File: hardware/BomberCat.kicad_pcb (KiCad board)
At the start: 2 copper layers, 65 x 84.7 mm, 111 parts, among them J1 Battery, J3 MAGSPOOF, J4 MAGSPOOF, P1 USB_C_Plug_USB2.0, Q1 DMG3415U-7, SW1 RESET, SW2 GPIO, SW3 ON, SW4 SOURCE MAG, U1 PN7150B0HN_C11002E-PN7150B0HN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

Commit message: fix(hw):update labels
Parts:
- removed kibuzzard-62EEB073: G***, kibuzzard-62EEB073
- removed kibuzzard-64382690: G***, kibuzzard-64382690
- added kibuzzard-67FEA661: G***, kibuzzard-67FEA661, B.Cu at (108.3, 145.5)
- added kibuzzard-67FEA7C0: G***, kibuzzard-67FEA7C0, B.Cu at (147.3, 150.3)

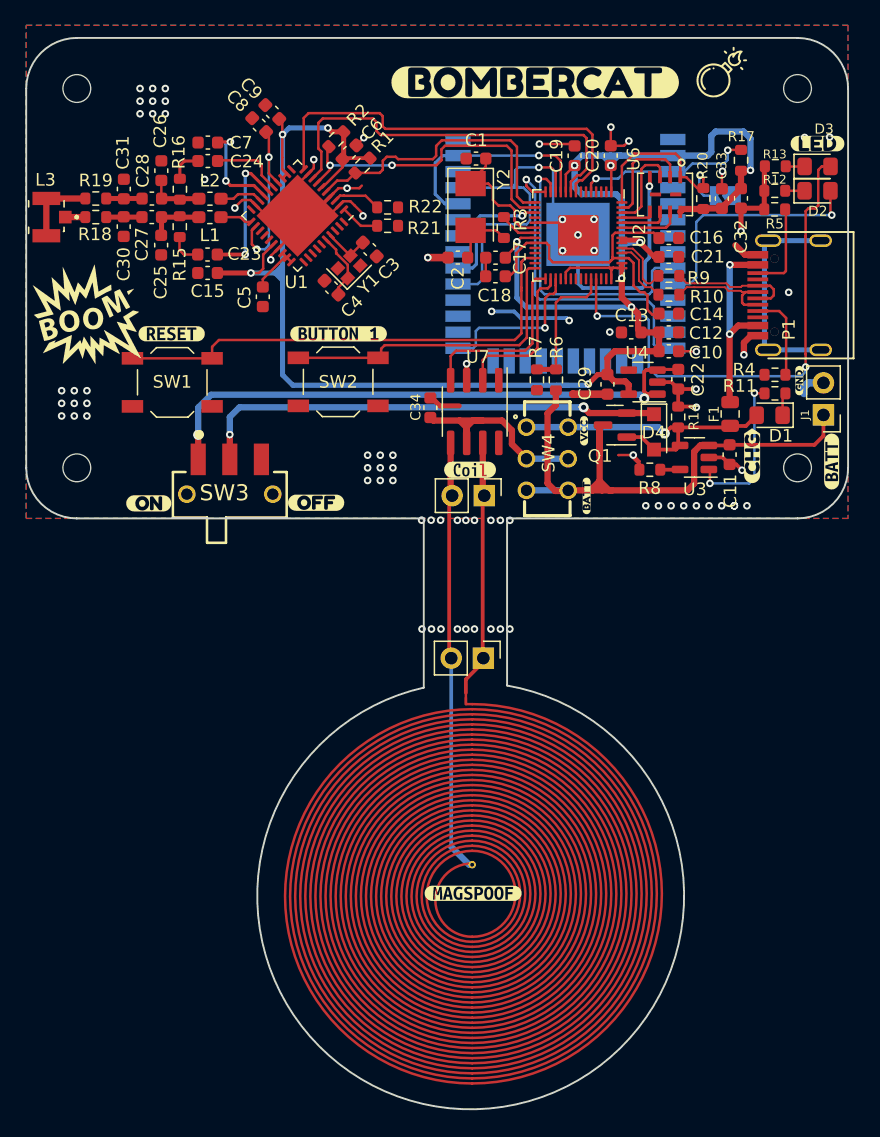
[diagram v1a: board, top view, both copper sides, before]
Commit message: feat(hw): update tracks, remove switch position change and resize coil arm,
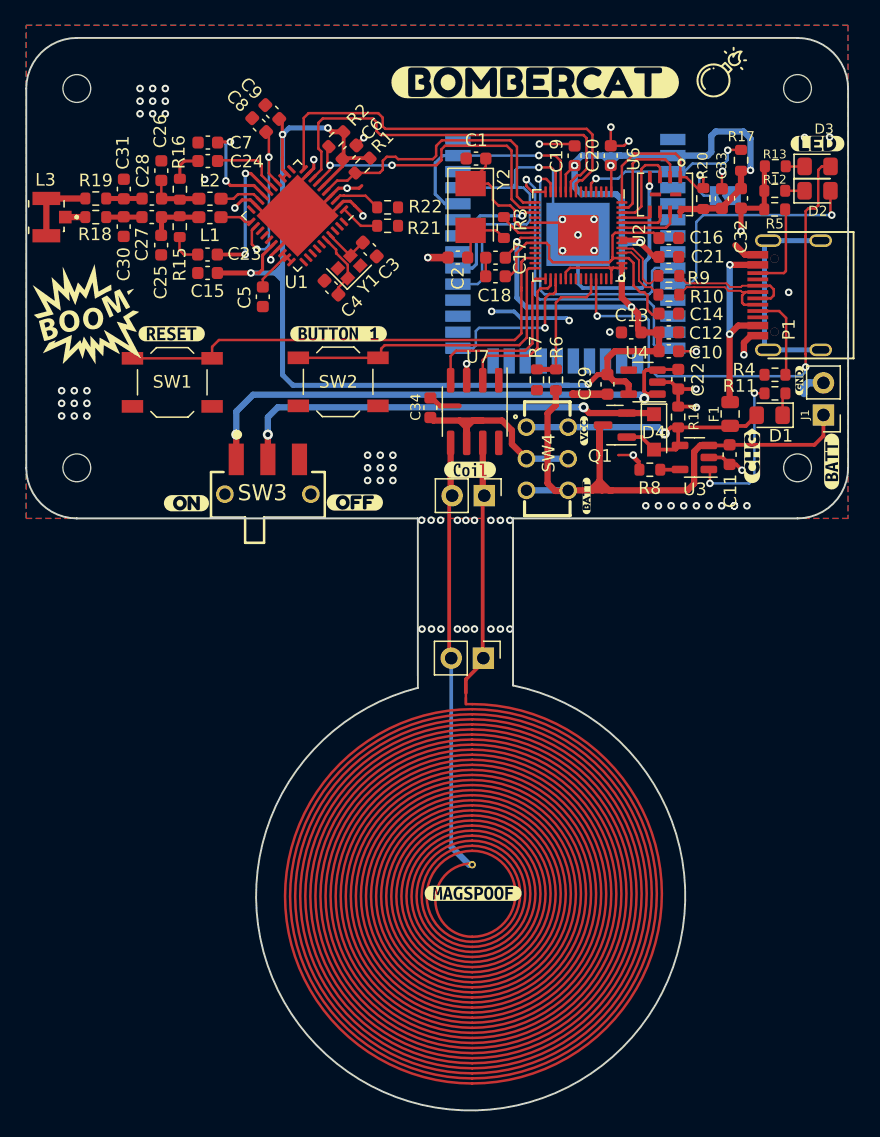
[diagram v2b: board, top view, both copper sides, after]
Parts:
- moved kibuzzard-67F6E601 3.06 mm to (118.0, 172.7)
- moved SW3 3.01 mm to (111.1, 170.3)
- moved kibuzzard-67F6E5D9 2.98 mm to (104.7, 172.8)
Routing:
- net Net-(SW3-A): track 46.6 -> 43.4 mm
- net Net-(D4-K): track 37.4 -> 34.5 mm
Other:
- board size 65 x 84.7 mm -> 65 x 84.8 mm

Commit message: fix(hw): update tracks width
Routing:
- net GND: track 124.8 -> 122.5 mm
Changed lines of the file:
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@@
 				(font
 					(size 0.001 0.001)
+					(thickness 0.15)
 				)
 				(justify mirror)
@@
 				(font
 					(size 0.001 0.001)
+					(thickness 0.15)
 				)
 				(justify mirror)
@@
 				(font
 					(size 0.001 0.001)
+					(thickness 0.15)
 				)
 				(justify mirror)
@@
 				(font
 					(size 0.001 0.001)
+					(thickness 0.15)
 				)
 				(justify mirror)
@@
 	)
 	(segment
+		(start 140.494216 169.474216)
+		(end 140.01 168.99)
+		(width 0.2)
+		(layer "F.Cu")
+		(net 2)
+	)
+	(segment
 		(start 126.835 161.775)
 		(end 126.83 161.77)
@@
 	)
 	(segment
-		(start 140.494216 170.149118)
-		(end 140.494216 169.474216)
-		(width 0.2)
-		(layer "F.Cu")
-		(net 2)
-	)
-	(segment
 		(start 123.761618 153.371618)
 		(end 123.76 153.37)
@@
 	)
 	(segment
-		(start 138.854216 168.989118)
-		(end 138.849216 168.994118)
-		(width 0.2)
-		(layer "F.Cu")
-		(net 2)
-	)
-	(segment
 		(start 109.735126 148.81)
 		(end 109.09 148.81)
@@
 	)
 	(segment
+		(start 140.494216 170.149118)
+		(end 140.494216 169.474216)
+		(width 0.2)
+		(layer "F.Cu")
+		(net 2)
+	)
+	(segment
 		(start 125.361716 153.371618)
 		(end 123.761618 153.371618)
@@
 	)
 	(segment
-		(start 140.494216 169.474216)
-		(end 140.01 168.99)
-		(width 0.2)
-		(layer "F.Cu")
-		(net 2)
-	)
-	(segment
-		(start 139.749216 168.989118)
-		(end 138.854216 168.989118)
-		(width 0.2)
-		(layer "F.Cu")
-		(net 2)
-	)
-	(segment
 		(start 141.919216 163.219118)
 		(end 143.019216 163.219118)
@@
 	)
 	(segment
-		(start 140.494216 170.149118)
-		(end 140.494216 169.734118)
-		(width 0.2)
-		(layer "F.Cu")
-		(net 2)
-	)
-	(segment
 		(start 124.714 165.1)
 		(end 126.238 165.1)
@@
 	)
 	(segment
-		(start 140.494216 169.734118)
-		(end 139.749216 168.989118)
-		(width 0.2)
-		(layer "F.Cu")
-		(net 2)
-	)
-	(segment
 		(start 111.913204 152.667456)
 		(end 113.46 151.12066)
@@
 		(start 155.05 167.47)
 		(end 155.05 165.82)
-		(width 0.3)
+		(width 0.5)
 		(layer "F.Cu")
 		(net 10)
@@
 		(start 145.986716 168.229118)
 		(end 147.579216 168.229118)
-		(width 0.3)
+		(width 0.5)
 		(layer "F.Cu")
 		(net 10)
@@
 		(start 147.629216 168.179118)
 		(end 154.340882 168.179118)
-		(width 0.3)
+		(width 0.5)
 		(layer "F.Cu")
 		(net 10)
@@
 		(start 154.340882 168.179118)
 		(end 155.05 167.47)
-		(width 0.3)
+		(width 0.5)
 		(layer "F.Cu")
 		(net 10)
@@
 		(start 147.579216 168.229118)
 		(end 147.629216 168.179118)
-		(width 0.3)
+		(width 0.5)
 		(layer "F.Cu")
 		(net 10)
@@
 		(start 142.975882 166.804118)
 		(end 142.5 167.28)
-		(width 0.3)
+		(width 0.5)
 		(layer "F.Cu")
 		(net 22)
@@
 		(start 143.381716 168.559118)
 		(end 143.711716 168.229118)
-		(width 0.3)
+		(width 0.5)
 		(layer "F.Cu")
 		(net 22)
@@
 		(start 141.649216 168.559118)
 		(end 143.381716 168.559118)
-		(width 0.3)
+		(width 0.5)
 		(layer "F.Cu")
 		(net 22)
@@
 		(start 143.559216 166.804118)
 		(end 142.975882 166.804118)
-		(width 0.3)
+		(width 0.5)
 		(layer "F.Cu")
 		(net 22)
@@
 		(start 139.496716 167.569118)
 		(end 140.659216 167.569118)
-		(width 0.3)
+		(width 0.5)
 		(layer "F.Cu")
 		(net 22)
@@
 		(start 148.920882 166.689118)
 		(end 149.77 165.84)
-		(width 0.3)
+		(width 0.5)
 		(layer "F.Cu")
 		(net 22)
@@
 		(start 147.514216 166.804118)
 		(end 147.629216 166.689118)
-		(width 0.3)
+		(width 0.5)
 		(layer "F.Cu")
 		(net 22)
@@
 		(start 140.659216 167.569118)
 		(end 141.649216 168.559118)
-		(width 0.3)
+		(width 0.5)
 		(layer "F.Cu")
 		(net 22)
@@
 		(start 143.559216 166.804118)
 		(end 143.559216 168.076618)
-		(width 0.3)
+		(width 0.5)
 		(layer "F.Cu")
 		(net 22)
@@
 		(start 143.559216 166.804118)
 		(end 147.514216 166.804118)
-		(width 0.3)
+		(width 0.5)
 		(layer "F.Cu")
 		(net 22)
@@
 		(start 147.629216 166.689118)
 		(end 148.920882 166.689118)
-		(width 0.3)
+		(width 0.5)
 		(layer "F.Cu")
 		(net 22)
@@
 		(start 143.559216 168.076618)
 		(end 143.711716 168.229118)
-		(width 0.3)
+		(width 0.5)
 		(layer "F.Cu")
 		(net 22)
@@
 		(start 151.82 165.84)
 		(end 151.82 164.33)
-		(width 0.2)
+		(width 0.25)
 		(layer "F.Cu")
 		(net 23)
@@
 		(start 151.82 164.33)
 		(end 152.04 164.11)
-		(width 0.2)
+		(width 0.25)
 		(layer "F.Cu")
 		(net 23)

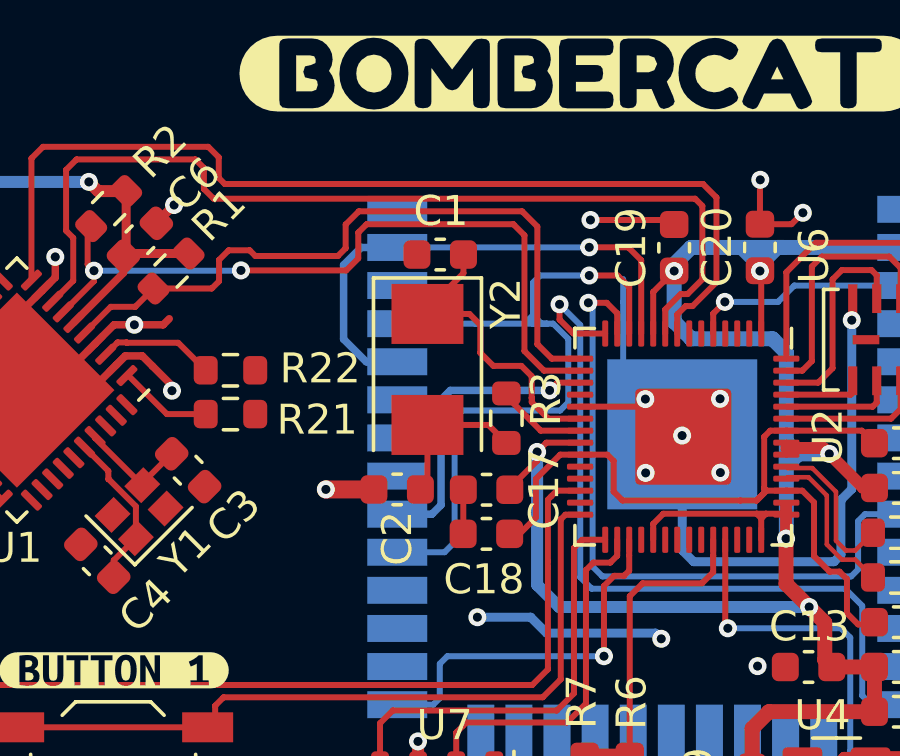
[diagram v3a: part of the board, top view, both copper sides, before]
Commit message: feat(Hw):Update_BoM
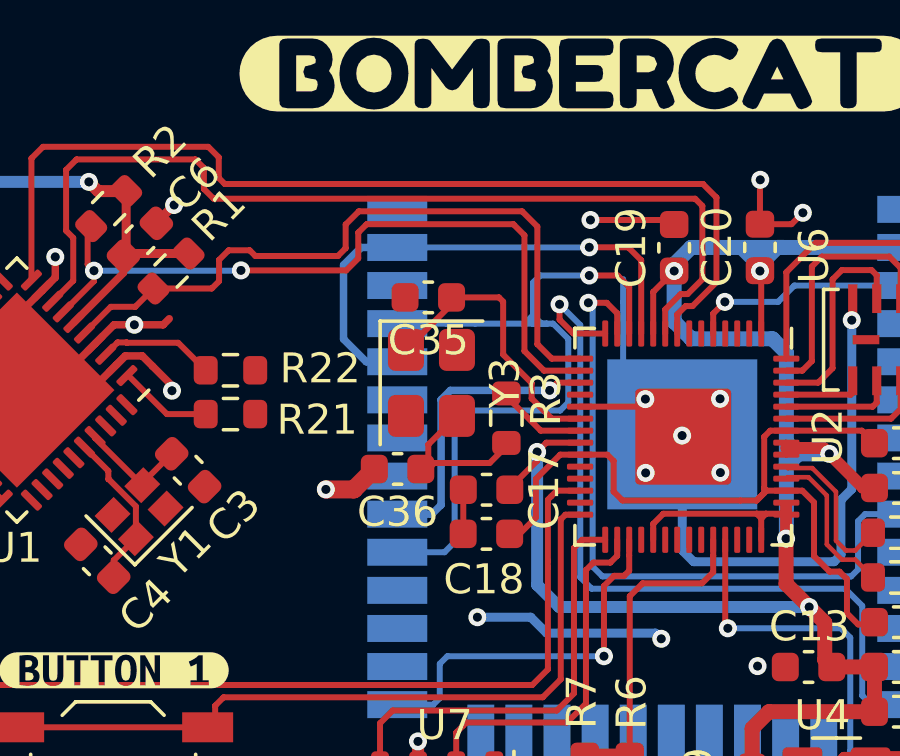
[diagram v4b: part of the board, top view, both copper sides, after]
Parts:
- removed C1, C2: 27pF, Capacitor_SMD:C_0603_1608Metric
- removed Y2: 12Mhz, Crystal:Crystal_SMD_5032-2Pin_5.0x3.2mm
- added C35: 15pF, Capacitor_SMD:C_0603_1608Metric, F.Cu at (127.2, 147.0)
- added C36: 15pF, Capacitor_SMD:C_0603_1608Metric, F.Cu at (126.2, 152.7)
- added Y3: ABM8-272-T3, Crystal:Crystal_SMD_Abracon_ABM8G-4Pin_3.2x2.5mm, F.Cu at (127.3, 149.8)
- C34: value 10uf -> 10uF
- U1: value PN7150B0HN_C11002E-PN7150B0HN_C11002E -> PN7150B0HN_C11006Y-PN7150B0HN_C11006Y

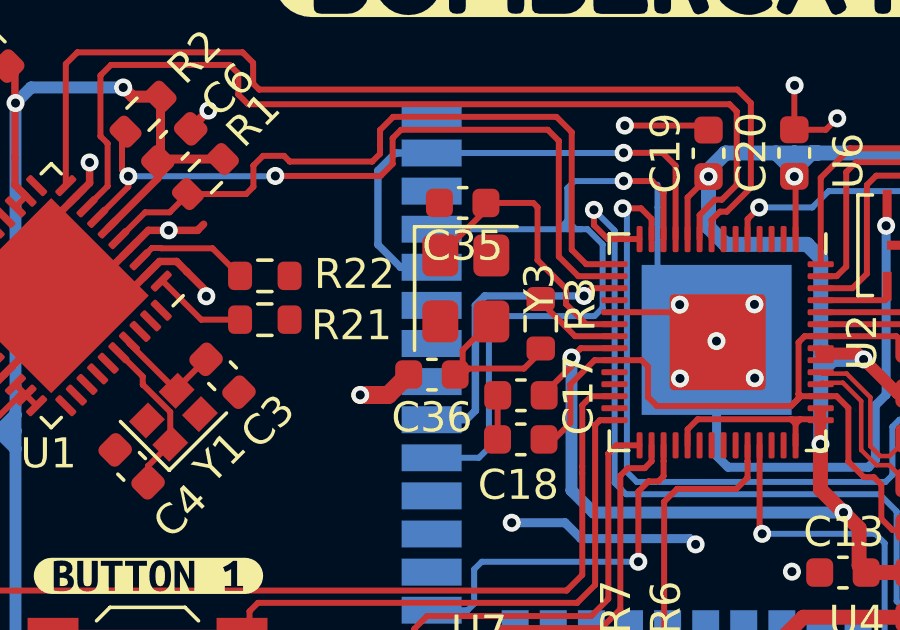
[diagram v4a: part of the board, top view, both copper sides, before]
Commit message: feat(hw): update Y3 footprint
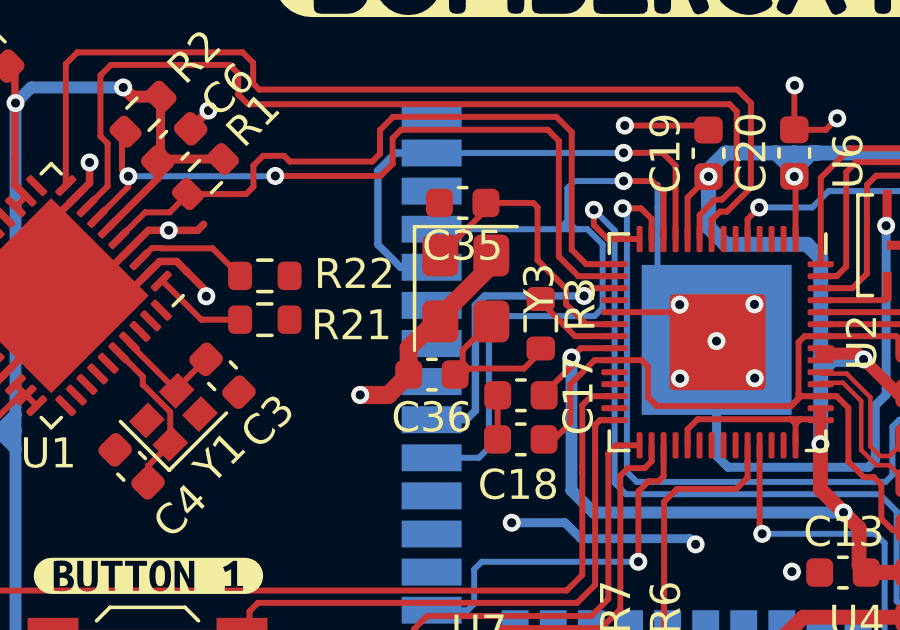
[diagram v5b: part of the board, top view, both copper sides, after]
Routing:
- net GND: track 122.8 -> 127.9 mm
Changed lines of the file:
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@@
 			(psa4output no)
 			(plot_black_and_white yes)
+			(plotinvisibletext no)
 			(sketchpadsonfab no)
 			(plotpadnumbers no)
@@
 		)
 		(pad "2" smd roundrect
+			(at -1.1 -0.85 270)
+			(size 1.4 1.2)
+			(layers "F.Cu" "F.Mask" "F.Paste")
+			(roundrect_rratio 0.208333)
+			(net 2 "GND")
+			(pinfunction "2")
+			(pintype "passive")
+		)
+		(pad "2" smd roundrect
 			(at 1.1 0.85 270)
 			(size 1.4 1.2)
@@
 			(pintype "passive")
 		)
-		(pad "4" smd roundrect
-			(at -1.1 -0.85 270)
-			(size 1.4 1.2)
-			(layers "F.Cu" "F.Mask" "F.Paste")
-			(roundrect_rratio 0.208333)
-		)
 		(embedded_fonts no)
 		(model "${KICAD9_3DMODEL_DIR}/Crystal.3dshapes/Crystal_SMD_Abracon_ABM8G-4Pin_3.2x2.5mm.step"
@@
 	)
 	(segment
+		(start 128.13 149.050998)
+		(end 128.13 148.72)
+		(width 0.6)
+		(layer "F.Cu")
+		(net 2)
+	)
+	(segment
 		(start 140.494216 170.149118)
 		(end 140.494216 169.474216)
@@
 	)
 	(segment
+		(start 125.375 151.805998)
+		(end 128.13 149.050998)
+		(width 0.6)
+		(layer "F.Cu")
+		(net 2)
+	)
+	(segment
 		(start 117.640162 148.920162)
 		(end 117.98 149.26)
@@
 		(layer "F.Cu")
 		(net 2)
+	)
+	(segment
+		(start 125.375 152.69)
+		(end 125.375 151.805998)
+		(width 0.6)
+		(layer "F.Cu")
+		(net 2)

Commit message: fix(Hw):PN7150_Updated
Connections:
- C35 pad 1: Net-(U2-XIN) -> Net-(U2-GPIO14)
- R3 pad 2: Net-(U2-XOUT) -> Net-(U2-GPIO16)
- U2 pad 10: +3V3 -> unconnected-(U2-IOVDD-Pad10)
- U2 pad 11: /CIPO_TX -> unconnected-(U2-GPIO8-Pad11)
- U2 pad 12: /CS_RX -> unconnected-(U2-GPIO9-Pad12)
- U2 pad 13: /ACK_CTS -> unconnected-(U2-GPIO10-Pad13)
- U2 pad 14: /COPI_RTS -> unconnected-(U2-GPIO11-Pad14)
- U2 pad 15: /SDA -> unconnected-(U2-GPIO12-Pad15)
- U2 pad 16: /SCL -> unconnected-(U2-GPIO13-Pad16)
- U2 pad 17: /SCK -> Net-(U2-GPIO14)
- U2 pad 19: GND -> unconnected-(U2-TESTEN-Pad19)
- U2 pad 20: Net-(U2-XIN) -> /SCK
- U2 pad 21: Net-(U2-XOUT) -> unconnected-(U2-XOUT-Pad21)
- U2 pad 23: +1V2 -> unconnected-(U2-DVDD-Pad23)
- U2 pad 24: /SWCLK -> unconnected-(U2-SWCLK-Pad24)
- U2 pad 25: /SWDIO -> unconnected-(U2-SWD-Pad25)
- U2 pad 26: /RST -> unconnected-(U2-RUN-Pad26)
- U2 pad 27: unconnected-(U2-GPIO16-Pad27) -> Net-(U2-GPIO16)
- U2 pad 28: /GPIO1 -> unconnected-(U2-GPIO17-Pad28)
- U2 pad 29: /IN_B -> unconnected-(U2-GPIO18-Pad29)
- U2 pad 30: /IN_A -> unconnected-(U2-GPIO19-Pad30)
- U2 pad 31: /ESP_GPIO0 -> unconnected-(U2-GPIO20-Pad31)
- U2 pad 32: unconnected-(U2-GPIO21-Pad32) -> /RST
- U2 pad 38: /B_ADC -> unconnected-(U2-GPIO26_ADC0-Pad38)
- U2 pad 39: /LED1 -> unconnected-(U2-GPIO27_ADC1-Pad39)
- U2 pad 4: unconnected-(U2-GPIO2-Pad4) -> /QSPI_DATA0
- U2 pad 43: +3V3 -> unconnected-(U2-ADC_AVDD-Pad43)
- U2 pad 45: +1V2 -> +3V3
- U2 pad 46: /RD- -> unconnected-(U2-USB_DM-Pad46)
- U2 pad 47: /RD+ -> unconnected-(U2-USB_DP-Pad47)
- U2 pad 48: +3V3 -> +1V2
- U2 pad 5: /ESP_RESET -> /QSPI_DATA1
- U2 pad 50: +1V2 -> unconnected-(U2-DVDD-Pad50)
- U2 pad 51: /QSPI_DATA3 -> unconnected-(U2-QSPI_SD3-Pad51)
- U2 pad 52: /QSPI_SCK -> unconnected-(U2-QSPI_SCLK-Pad52)
- U2 pad 53: /QSPI_DATA0 -> unconnected-(U2-QSPI_SD0-Pad53)
- U2 pad 54: /QSPI_DATA2 -> unconnected-(U2-QSPI_SD2-Pad54)
- U2 pad 55: /QSPI_DATA1 -> /ESP_RESET
- U2 pad 56: /QSPI_CS -> unconnected-(U2-QSPI_SS-Pad56)
- U2 pad 6: unconnected-(U2-GPIO4-Pad6) -> /QSPI_DATA2
- U2 pad 7: unconnected-(U2-GPIO5-Pad7) -> /QSPI_DATA3
- U2 pad 8: /VEN -> unconnected-(U2-GPIO6-Pad8)
- U2 pad 9: /IRQ -> unconnected-(U2-GPIO7-Pad9)
- Y3 pad 1: Net-(U2-XIN) -> Net-(U2-GPIO14)
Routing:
- net Net-(U2-XIN): track 9.67 -> 0.00 mm
- net /SCK: track 9.97 -> 19.6 mm
- net Net-(U2-XOUT): track 3.03 -> 0.00 mm
- net (no net): track 0.00 -> 3.03 mm
